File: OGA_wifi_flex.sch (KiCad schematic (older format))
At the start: 8 parts, among them J1 5034802000, U1 OGA_ESP-12E

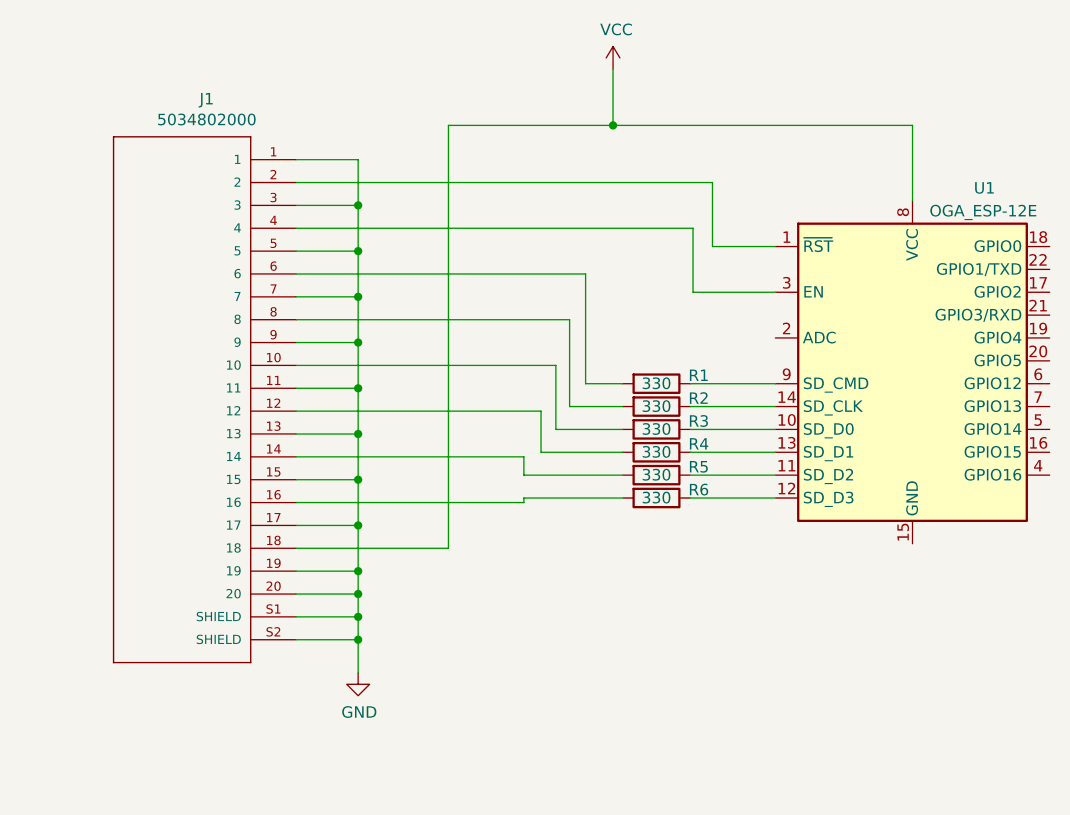
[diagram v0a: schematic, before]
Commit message: different pcb and sch for this branch
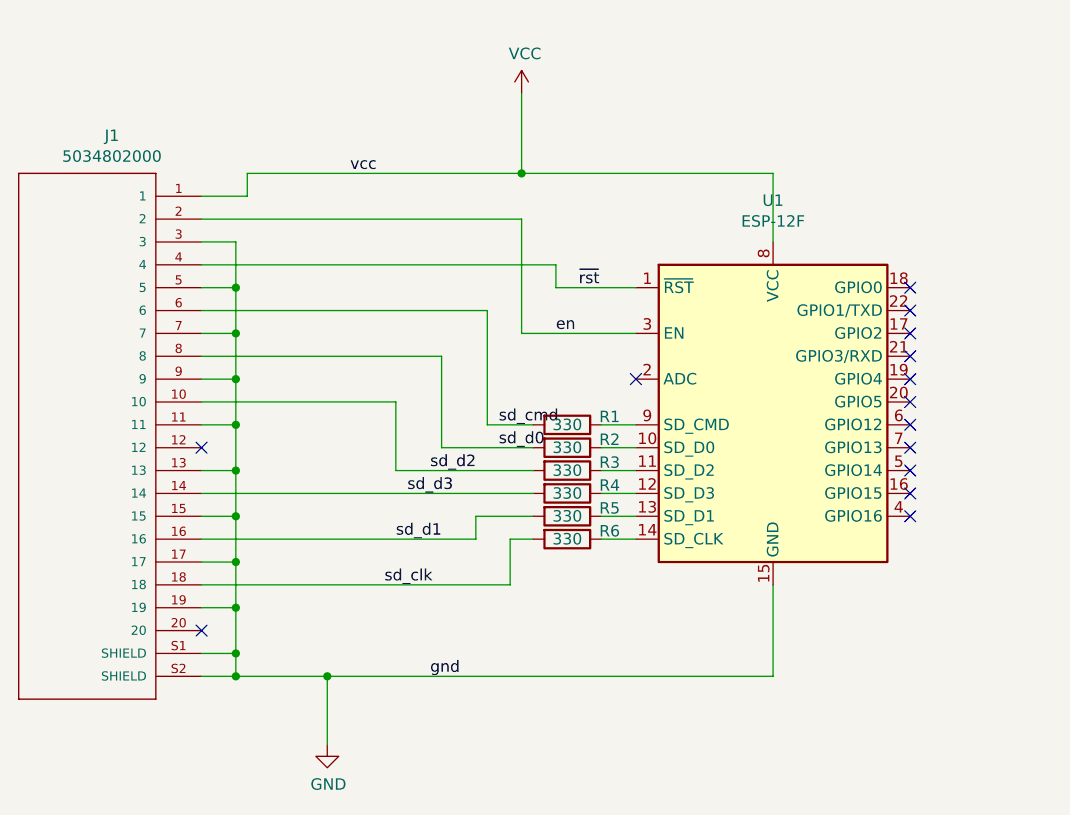
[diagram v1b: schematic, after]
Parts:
- removed U1: OGA_ESP-12E, RF_module:ESP-12E, symbol OGA_ESP12F:OGA_ESP-12E
- added U1: ESP-12F, RF_module:ESP-12E, symbol OGA_ESP12F:ESP-12F
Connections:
- net GND: now also U1.15 (GND); no longer J1.1, J1.20
- net VCC: now also J1.1, U1.8 (VCC); no longer J1.18
- net en: now reaches J1.2
- net en: now also U1.3 (EN)
- net at R3.1: now also U1.11 (SD_D2)
- net at R5.1: now also U1.13 (SD_D1)
- net at R6.1: now also U1.14 (SD_CLK)
- net at R4.1: now also U1.12 (SD_D3)
- net at R2.1: now also U1.10 (SD_D0)
- net ~rst: now reaches J1.4
- net ~rst: now also U1.1 (~RST)
- net at R1.1: now also U1.9 (SD_CMD)
- net sd_d2: now reaches J1.10, R3.2
- net at J1.12: no longer R4.2
- net sd_d1: now reaches R5.2
- net sd_d1: now also J1.16; no longer J1.14
- net sd_clk: now reaches R6.2
- net sd_clk: now also J1.18; no longer J1.16
- net sd_cmd: now reaches J1.6, R1.2
- net sd_d0: now reaches J1.8, R2.2
- new net sd_d3: J1.14, R4.2
- no-connect marks 0 -> 14
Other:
- moved on the sheet: J1, R1, R2, R3, R4, R5, R6
